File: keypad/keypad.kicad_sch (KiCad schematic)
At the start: 67 parts, among them J1 NO FIT, J2 NO FIT, P1 GT-USB-7010ASV, SW1 TS04-66-70-BK-100-SMT, SW2 TS04-66-70-BK-100-SMT, SW4 NO FIT, SW5 NO FIT, U1 RP2040, U2 LM4040DBZ-2.0, U3 W25Q16JVSSIQ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

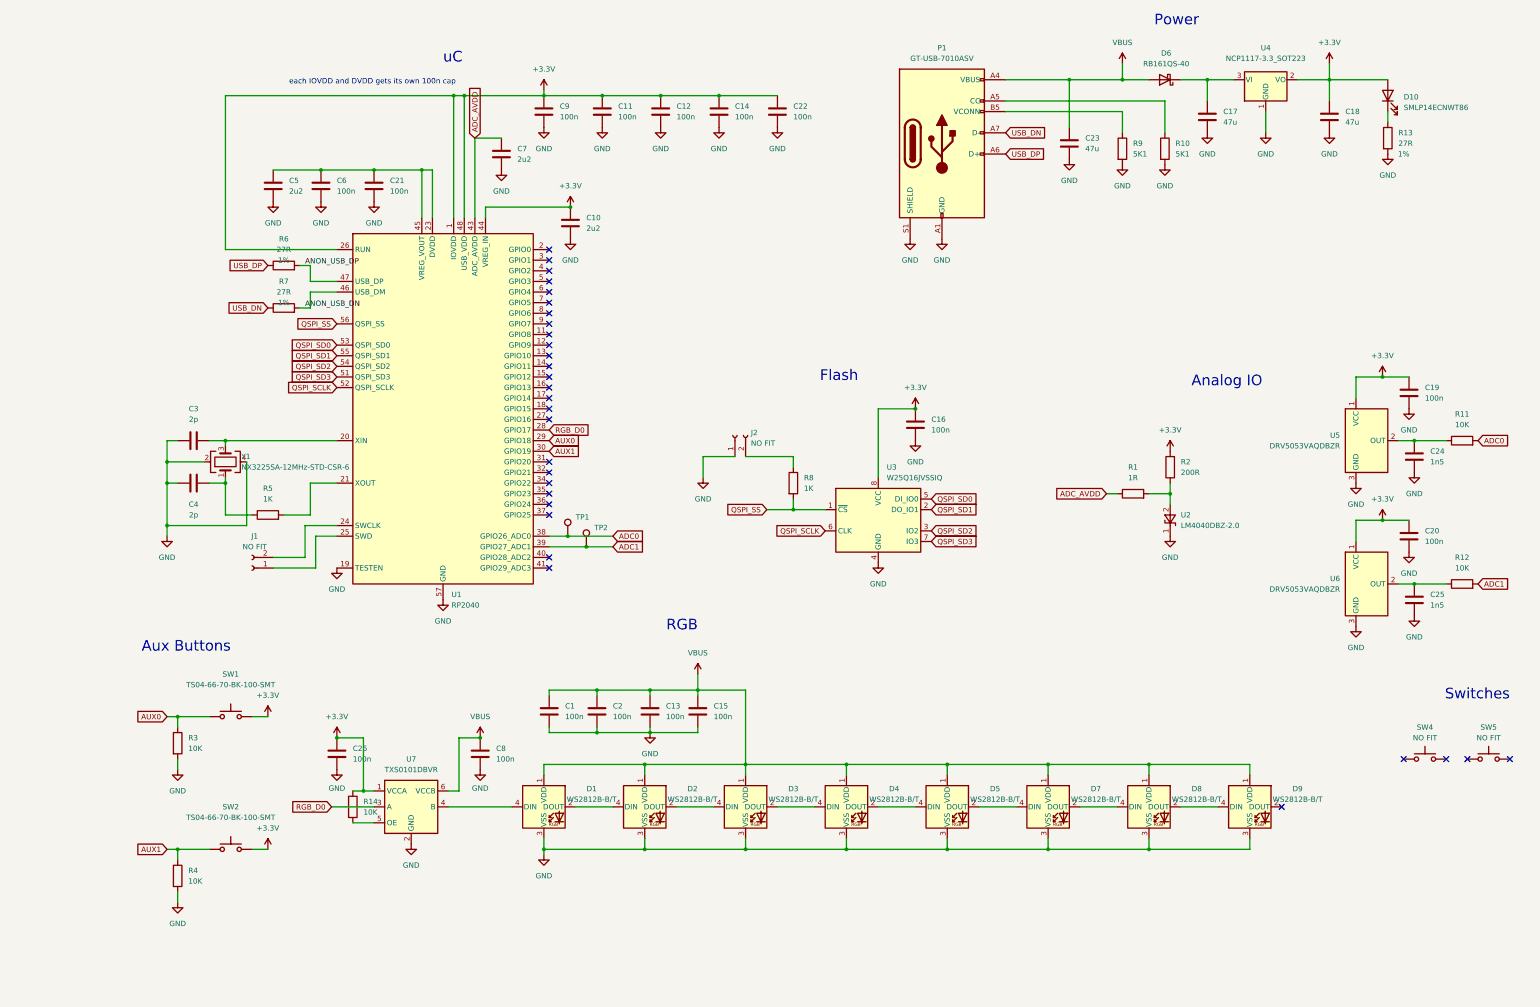
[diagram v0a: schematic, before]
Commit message: initial placements for rev3b
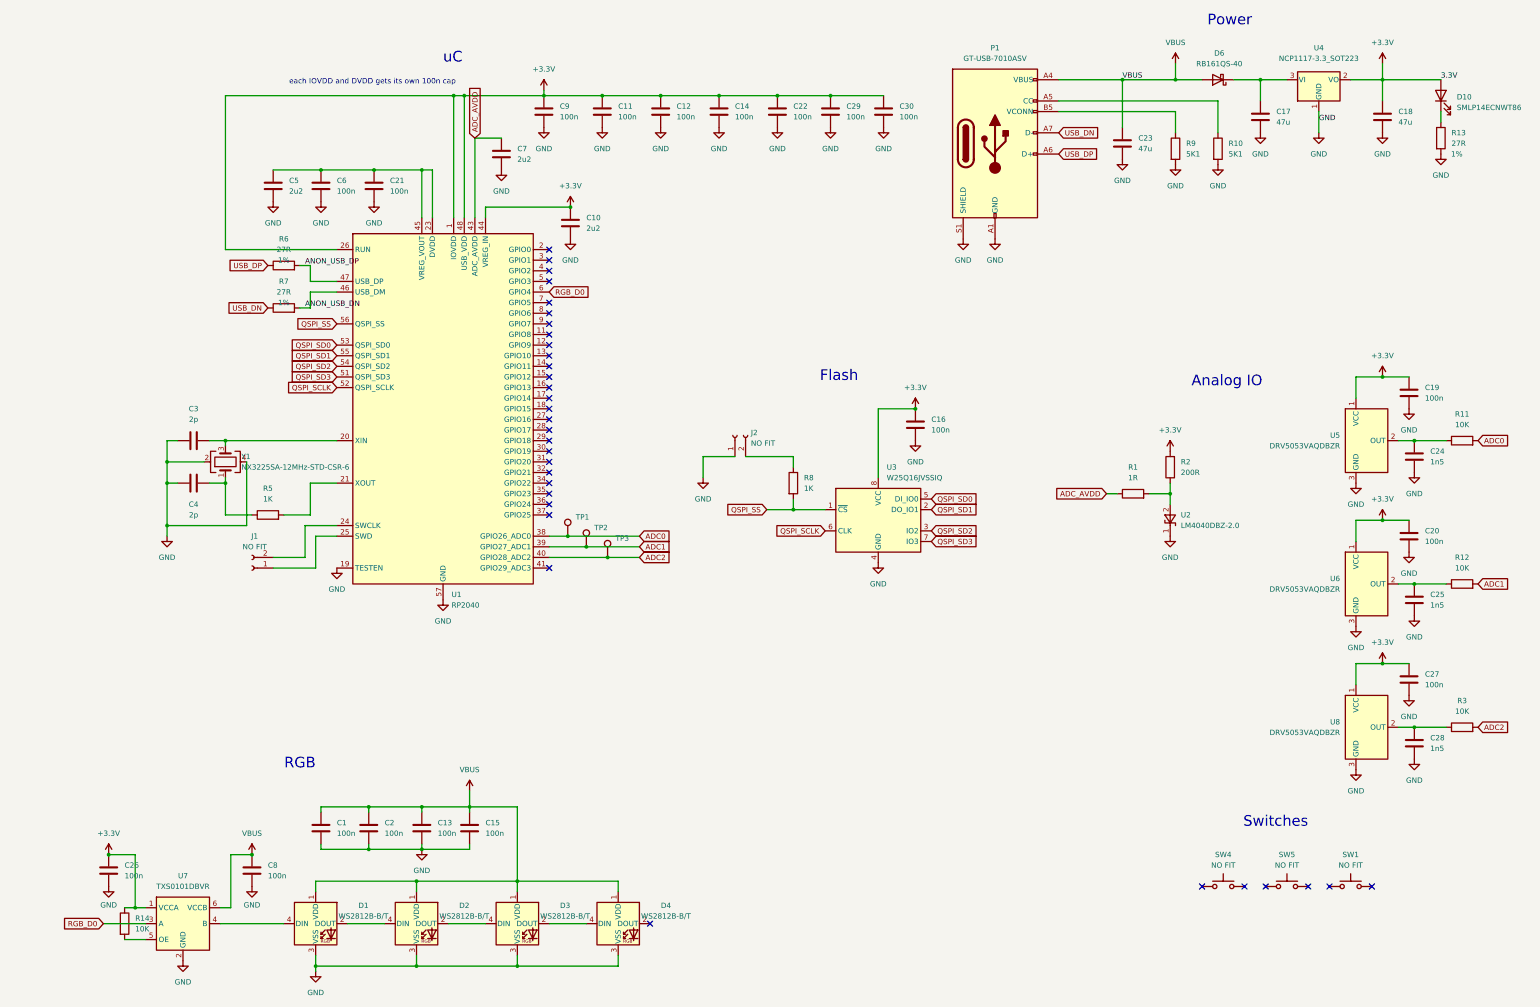
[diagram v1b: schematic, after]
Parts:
- removed D5, D7, D8, D9: WS2812B-B/T, LED_SMD:LED_WS2812B_PLCC4_5.0x5.0mm_P3.2mm, symbol LED:WS2812B
- removed R4: 10K, Resistor_SMD:R_0805_2012Metric, symbol Device:R
- removed SW2: TS04-66-70-BK-100-SMT, Button_Switch_SMD:SW_Push_1P1T_NO_6x6mm_H9.5mm, symbol Switch:SW_Push
- added C27, C29, C30: 100n, Capacitor_SMD:C_0805_2012Metric, symbol Device:C
- added C28: 1n5, Capacitor_SMD:C_0805_2012Metric, symbol Device:C
- added TP3: NO FIT, TestPoint:TestPoint_Pad_1.5x1.5mm, symbol Connector:TestPoint
- added U8: DRV5053VAQDBZR, Package_TO_SOT_SMD:SOT-23, symbol Sensor_Magnetic:DRV5033AJxDBZ
- SW1: value TS04-66-70-BK-100-SMT -> NO FIT; footprint Button_Switch_SMD:SW_Push_1P1T_NO_6x6mm_H9.5mm -> Button_Switch_Keyboard:SW_Cherry_MX_1.00u_PCB
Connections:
- net +3.3V: now also C27.1, C29.1, C30.1, U8.1 (VCC); no longer SW1.2
- net GND: now also C27.2, C28.2, C29.2, C30.2, U8.3 (GND); no longer R3.2
- net RGB_D0: now also U1.6 (GPIO4); no longer U1.28 (GPIO17)
- net ADC2: now reaches U1.40 (GPIO28_ADC2)
- net ADC2: now also R3.2, TP3.1
- removed net AUX0: R3.1, SW1.1, U1.29 (GPIO18)
- net AUX1: no longer names the net of U1.30 (GPIO19)
- new net: C28.1, R3.1, U8.2 (OUT)
- no-connect marks 30 -> 33
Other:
- note removed: "Aux Buttons"
- company: (none) -> cawlcitge
- title: (none) -> pppad rev3b
- moved on the sheet: C1, C13, C15, C17, C18, C2, C23, C26, C8, D1, D10, D2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

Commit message: finish rev3b
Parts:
- added R15, R4: 10K, Resistor_SMD:R_0805_2012Metric, symbol Device:R
- added SW2, SW3: TS04, Custom_Footprints:TS04, symbol Custom_Parts:TS04
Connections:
- net +3.3V: now also SW2.2, SW3.2
- net GND: now also R15.2, R4.2
- net AUX1: now reaches U1.7 (GPIO5)
- net AUX1: now also R15.1, SW3.1
- net AUX0: now reaches U1.8 (GPIO6)
- net AUX0: now also R4.1, SW2.1
- no-connect marks 33 -> 31
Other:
- note added: "Aux Buttons"
- moved on the sheet: C10, C11, C12, C14, C16, C21, C22, C29, C3, C30, C4, C5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
